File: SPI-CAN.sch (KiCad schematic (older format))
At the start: 11 parts, among them J1 Screw_Terminal_1x02, P11 CONN_01X02, P12 CONN_01X03, U6 MCP25625-E/SS, Y1 Crystal_Small

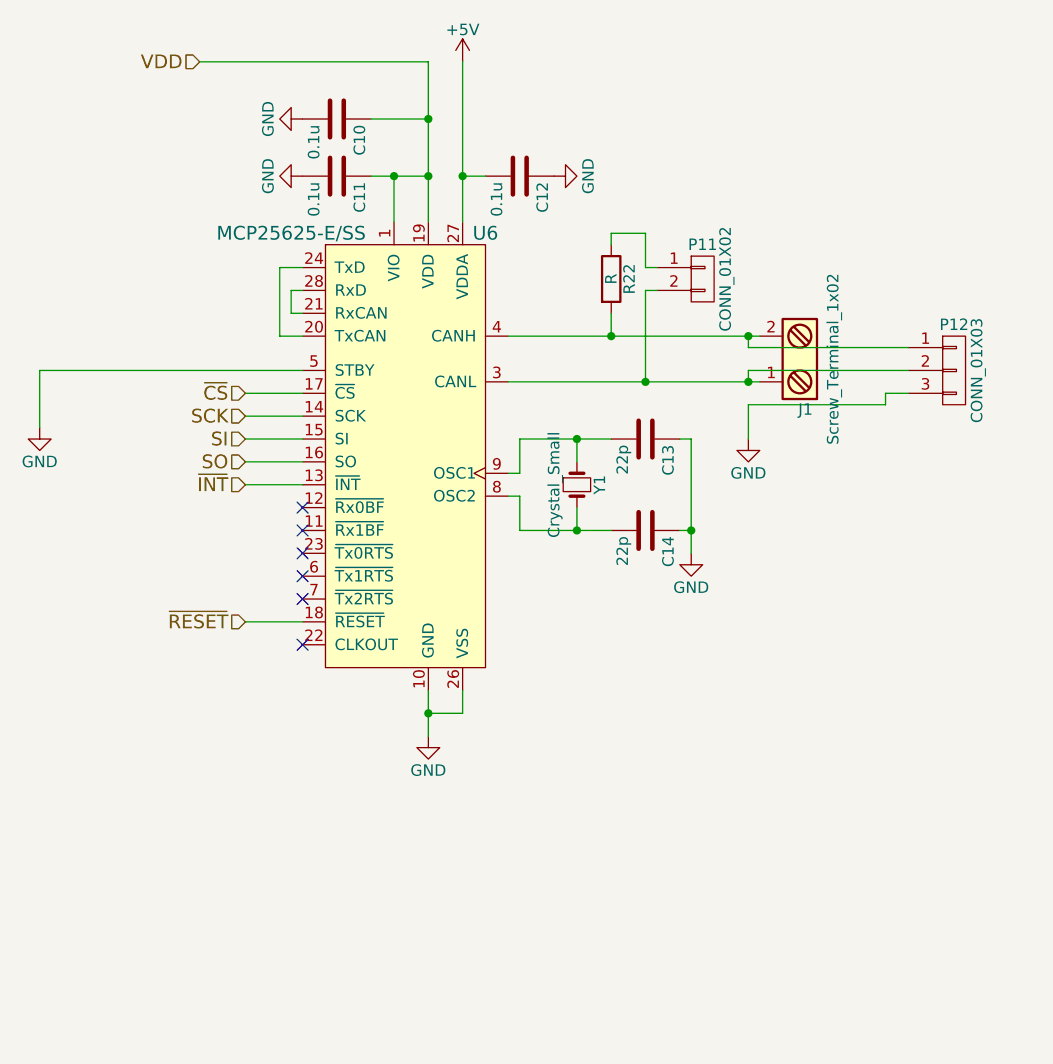
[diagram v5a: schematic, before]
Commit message: 図面にタイトルを追加
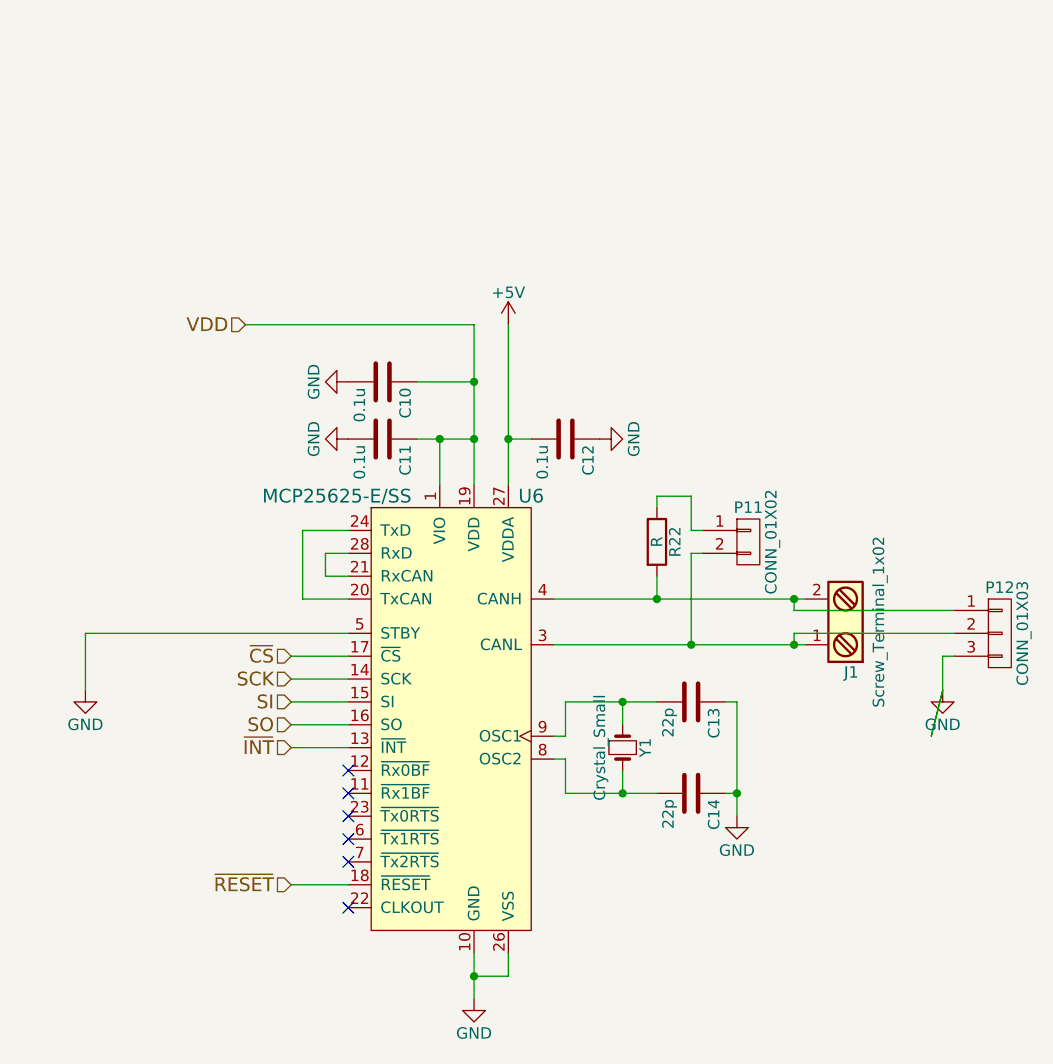
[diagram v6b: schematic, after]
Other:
- moved on the sheet: C10, C11, C12, C13, C14, J1, P11, P12, R22, U6, Y1

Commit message: 名称変更，再アノテーション
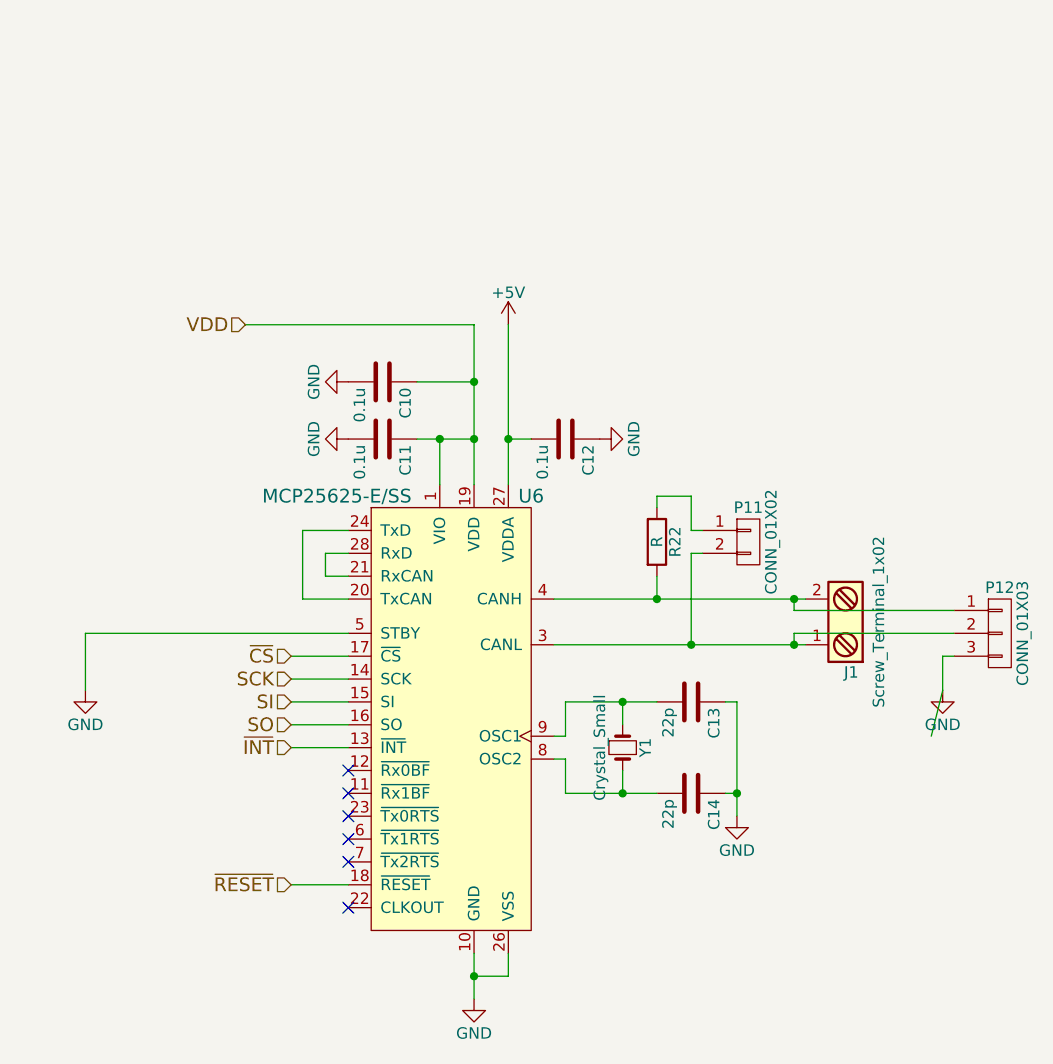
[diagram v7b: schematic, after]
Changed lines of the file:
@@
 encoding utf-8
 Sheet 4 5
-Title "JetsonTK1_GPIO_Connector"
+Title "JetsonTK1_Expand_Board"
 Date "2016-12-18"
 Rev "1.1"
@@
 	5100 5100 4850 5100
 Wire Wire Line
-	5650 5400 5650 5500
-Wire Wire Line
-	5650 5500 5650 5600
+	5650 5400 5650 5600
 Wire Wire Line
 	5800 5400 5800 5500
@@
 Connection ~ 5650 5500
 Wire Wire Line
-	6000 3850 6450 3850
-Wire Wire Line
-	6450 3850 7050 3850
-Wire Wire Line
-	7050 3850 7100 3850
-Wire Wire Line
-	6000 4050 6600 4050
-Wire Wire Line
-	6600 4050 7050 4050
-Wire Wire Line
-	7050 4050 7100 4050
+	6000 3850 7100 3850
+Wire Wire Line
+	6000 4050 7100 4050
 Wire Wire Line
 	7700 4250 7650 4450
@@
 Connection ~ 6450 3850
 Wire Wire Line
-	5800 2650 5800 3150
-Wire Wire Line
-	5800 3150 5800 3350
-Wire Wire Line
-	5650 2650 5650 2900
-Wire Wire Line
-	5650 2900 5650 3150
-Wire Wire Line
-	5650 3150 5650 3350
+	5800 2650 5800 3350
+Wire Wire Line
+	5650 2650 5650 3350
 Wire Wire Line
 	5650 2650 4650 2650
@@
 	5500 3350 5500 3150
 Wire Wire Line
-	5400 3150 5500 3150
-Wire Wire Line
-	5500 3150 5650 3150
+	5400 3150 5650 3150
 Connection ~ 5650 3150
 Connection ~ 5500 3150
@@
 	6050 4550 6050 4700
 Wire Wire Line
-	6050 4700 6300 4700
-Wire Wire Line
-	6300 4700 6450 4700
+	6050 4700 6450 4700
 Wire Wire Line
 	6300 4600 6300 4700
@@
 	6050 4450 6050 4300
 Wire Wire Line
-	6050 4300 6300 4300
-Wire Wire Line
-	6300 4300 6450 4300
+	6050 4300 6450 4300
 Wire Wire Line
 	6300 4300 6300 4400
@@
 	7700 4100 7700 4250
 Wire Wire Line
-	7700 4250 7650 4450
-Wire Wire Line
 	7750 4000 7050 4000
 Wire Wire Line
@@
 Connection ~ 7050 3850
 Wire Wire Line
-	6800 4300 6800 4700
-Wire Wire Line
-	6800 4700 6800 4800
+	6800 4300 6800 4800
 Connection ~ 6800 4700
 $EndSCHEMATC

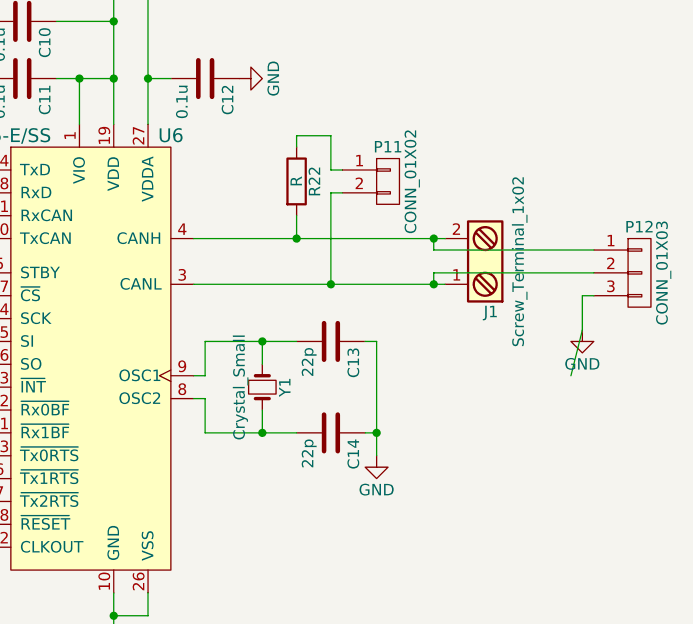
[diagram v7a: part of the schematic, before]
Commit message: 部品に定数を追加
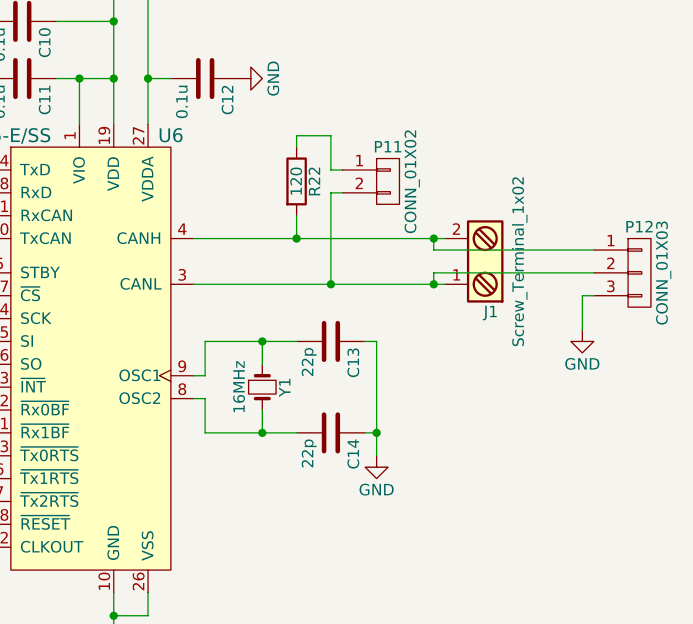
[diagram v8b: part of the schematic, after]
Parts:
- R22: value R -> 120
- Y1: value Crystal_Small -> 16MHz
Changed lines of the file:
@@
 Date "2016-12-18"
 Rev "1.1"
-Comp "Manju-Honpo"
+Comp "Manju-Hompo"
 Comment1 "@C91"
 Comment2 "Designed by @yuqlid"
@@
 P 6450 3600
 F 0 "R22" V 6530 3600 50  0000 C CNN
-F 1 "R" V 6450 3600 50  0000 C CNN
+F 1 "120" V 6450 3600 50  0000 C CNN
 F 2 "Resistors_SMD:R_0603" V 6380 3600 50  0001 C CNN
 F 3 "" H 6450 3600 50  0000 C CNN
@@
 P 6300 4500
 F 0 "Y1" H 6300 4600 50  0000 C CNN
-F 1 "Crystal_Small" H 6300 4400 50  0000 C CNN
+F 1 "16MHz" H 6300 4400 50  0000 C CNN
 F 2 "Crystals:Crystal_HC49-U_Vertical" H 6300 4500 50  0001 C CNN
 F 3 "" H 6300 4500 50  0000 C CNN
@@
 	6000 4050 7100 4050
 Wire Wire Line
-	7700 4250 7650 4450
-Wire Wire Line
 	6450 3450 6450 3400
